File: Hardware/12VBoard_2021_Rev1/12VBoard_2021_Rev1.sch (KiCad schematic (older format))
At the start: 0 parts

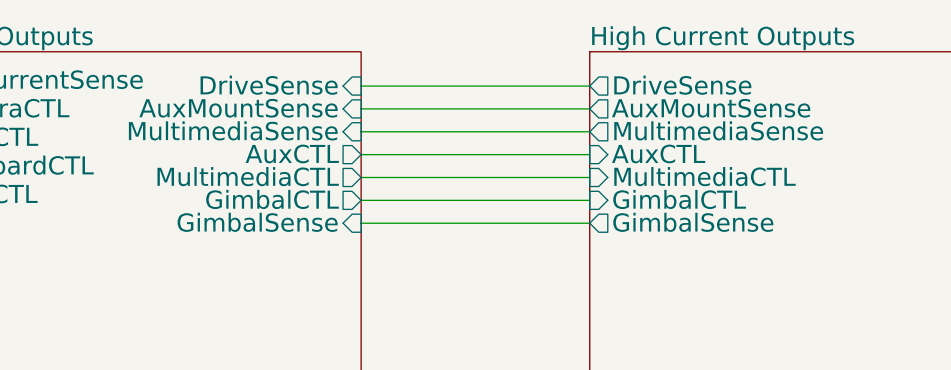
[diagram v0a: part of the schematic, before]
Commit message: Checked H pins
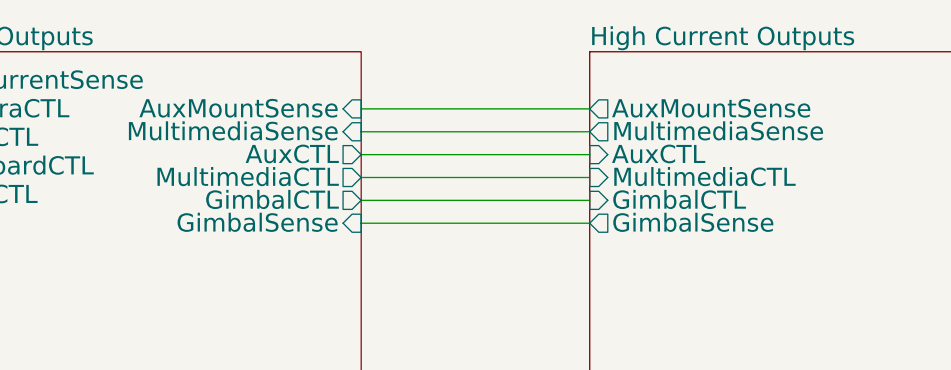
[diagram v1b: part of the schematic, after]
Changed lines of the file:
@@
 EESchema Schematic File Version 4
-LIBS:12VBoard_2021_Rev1-cache
 EELAYER 30 0
 EELAYER END
@@
 F2 "PackVoltage" I L 8000 3900 79
 F3 "5V" I L 8000 3625 79
-F4 "DriveSense" O L 8000 2150 79
-F5 "AuxMountSense" O L 8000 2250 79
-F6 "MultimediaSense" O L 8000 2350 79
-F7 "AuxCTL" I L 8000 2450 79
-F8 "MultimediaCTL" I L 8000 2550 79
-F9 "GimbalCTL" I L 8000 2650 79
-F10 "GimbalSense" O L 8000 2750 79
+F4 "AuxMountSense" O L 8000 2250 79
+F5 "MultimediaSense" O L 8000 2350 79
+F6 "AuxCTL" I L 8000 2450 79
+F7 "MultimediaCTL" I L 8000 2550 79
+F8 "GimbalCTL" I L 8000 2650 79
+F9 "GimbalSense" O L 8000 2750 79
 $EndSheet
 Wire Wire Line
@@
 	4000 2500 5000 2500
 Wire Wire Line
-	7000 2150 8000 2150
-Wire Wire Line
 	7000 2250 8000 2250
-Wire Wire Line
-	7000 2350 8000 2350
 Wire Wire Line
 	7000 2450 8000 2450
@@
 F0 "Tiva In/Outputs" 79
 F1 "Tiva.sch" 79
-F2 "DriveSense" I R 7000 2150 79
-F3 "LowCurrentSense" I L 5000 2125 79
-F4 "AuxMountSense" I R 7000 2250 79
-F5 "CameraCTL" O L 5000 2250 79
-F6 "MultimediaSense" I R 7000 2350 79
-F7 "NavBoardCTL" O L 5000 2500 79
-F8 "AuxCTL" O R 7000 2450 79
-F9 "MultimediaCTL" O R 7000 2550 79
-F10 "ExtraCTL" O L 5000 2625 79
-F11 "GimbalCTL" O R 7000 2650 79
-F12 "GimbalSense" I R 7000 2750 79
-F13 "DriveCTL" O L 5000 2375 79
+F2 "LowCurrentSense" I L 5000 2125 79
+F3 "AuxMountSense" I R 7000 2250 79
+F4 "CameraCTL" O L 5000 2250 79
+F5 "MultimediaSense" I R 7000 2350 79
+F6 "NavBoardCTL" O L 5000 2500 79
+F7 "AuxCTL" O R 7000 2450 79
+F8 "MultimediaCTL" O R 7000 2550 79
+F9 "ExtraCTL" O L 5000 2625 79
+F10 "GimbalCTL" O R 7000 2650 79
+F11 "GimbalSense" I R 7000 2750 79
+F12 "DriveCTL" O L 5000 2375 79
 $EndSheet
+Wire Wire Line
+	7000 2350 8000 2350
 $EndSCHEMATC

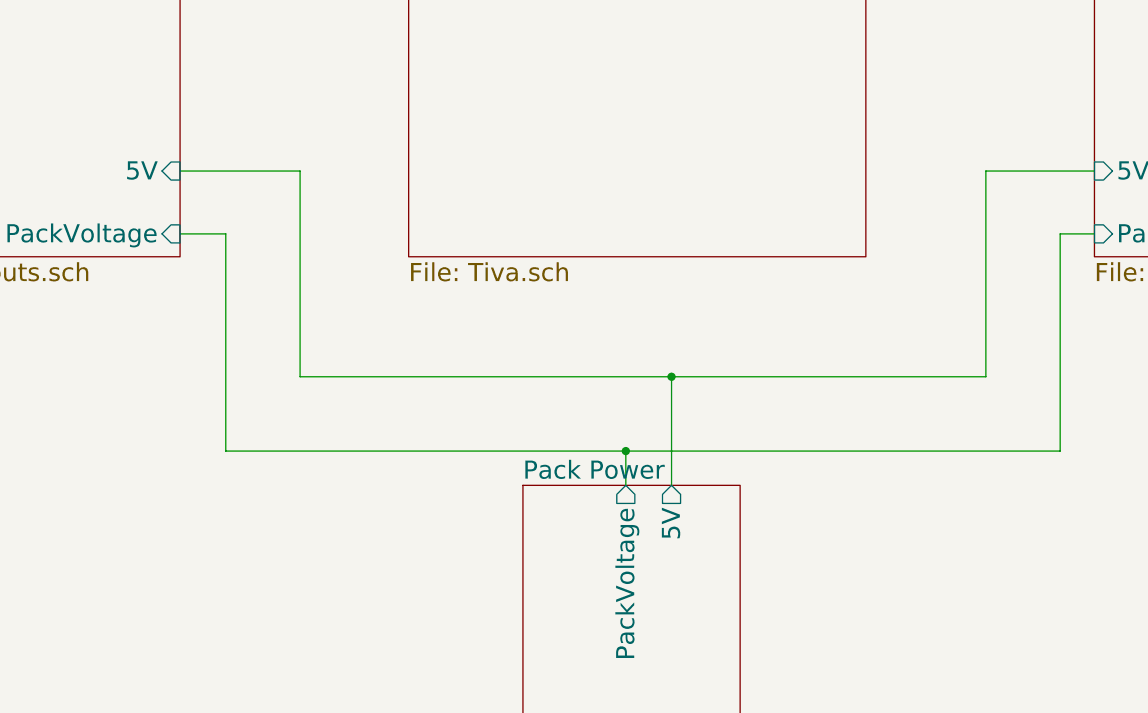
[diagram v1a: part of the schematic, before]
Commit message: Aded oki and started change of high side logic setup
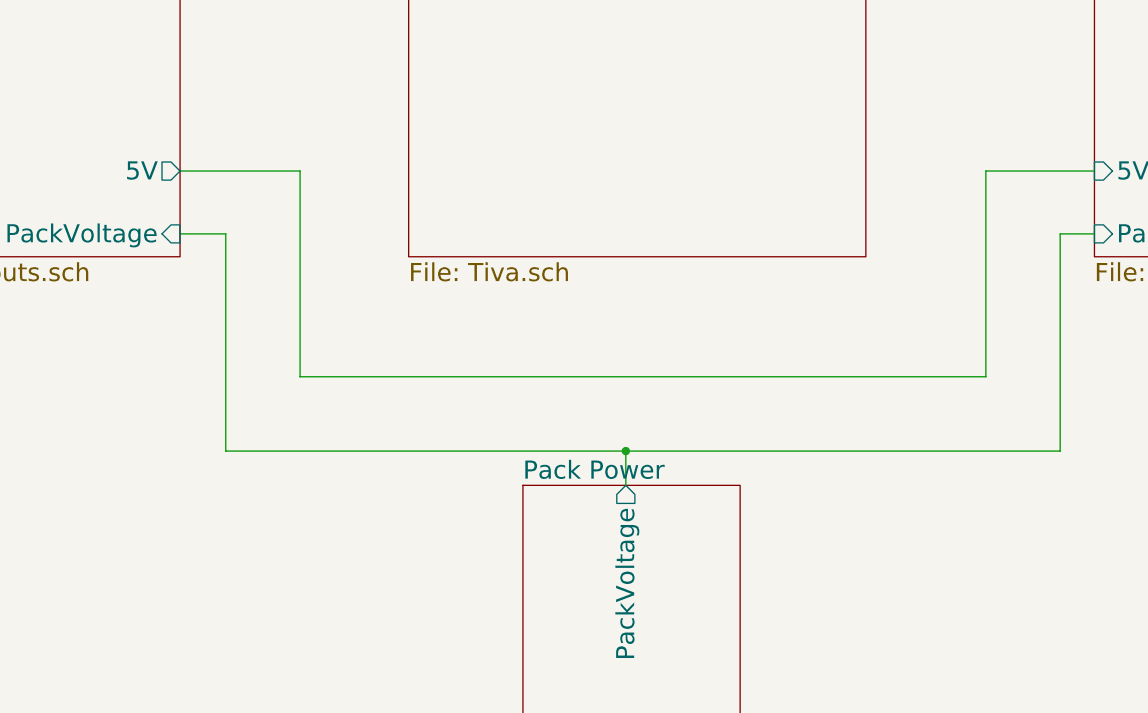
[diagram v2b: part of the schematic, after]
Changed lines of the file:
@@
 F1 "Pack Power.sch" 79
 F2 "PackVoltage" O T 5950 5000 79
-F3 "5V" O T 6150 5000 79
 $EndSheet
 Wire Wire Line
@@
 	7850 3900 8000 3900
 Wire Wire Line
-	6150 5000 6150 4525
-Wire Wire Line
-	6150 4525 4525 4525
-Wire Wire Line
 	4525 4525 4525 3625
 Wire Wire Line
 	4525 3625 4000 3625
-Wire Wire Line
-	6150 4525 7525 4525
-Connection ~ 6150 4525
 Wire Wire Line
 	7525 3625 8000 3625
@@
 F1 "Low Current Outputs.sch" 79
 F2 "PackVoltage" I R 4000 3900 79
-F3 "5V" I R 4000 3625 79
+F3 "5V" O R 4000 3625 79
 F4 "CameraToggle" I R 4000 2250 79
 F5 "NavToggle" I R 4000 2500 79
@@
 Wire Wire Line
 	7000 2350 8000 2350
+Wire Wire Line
+	4525 4525 7525 4525
 $EndSCHEMATC

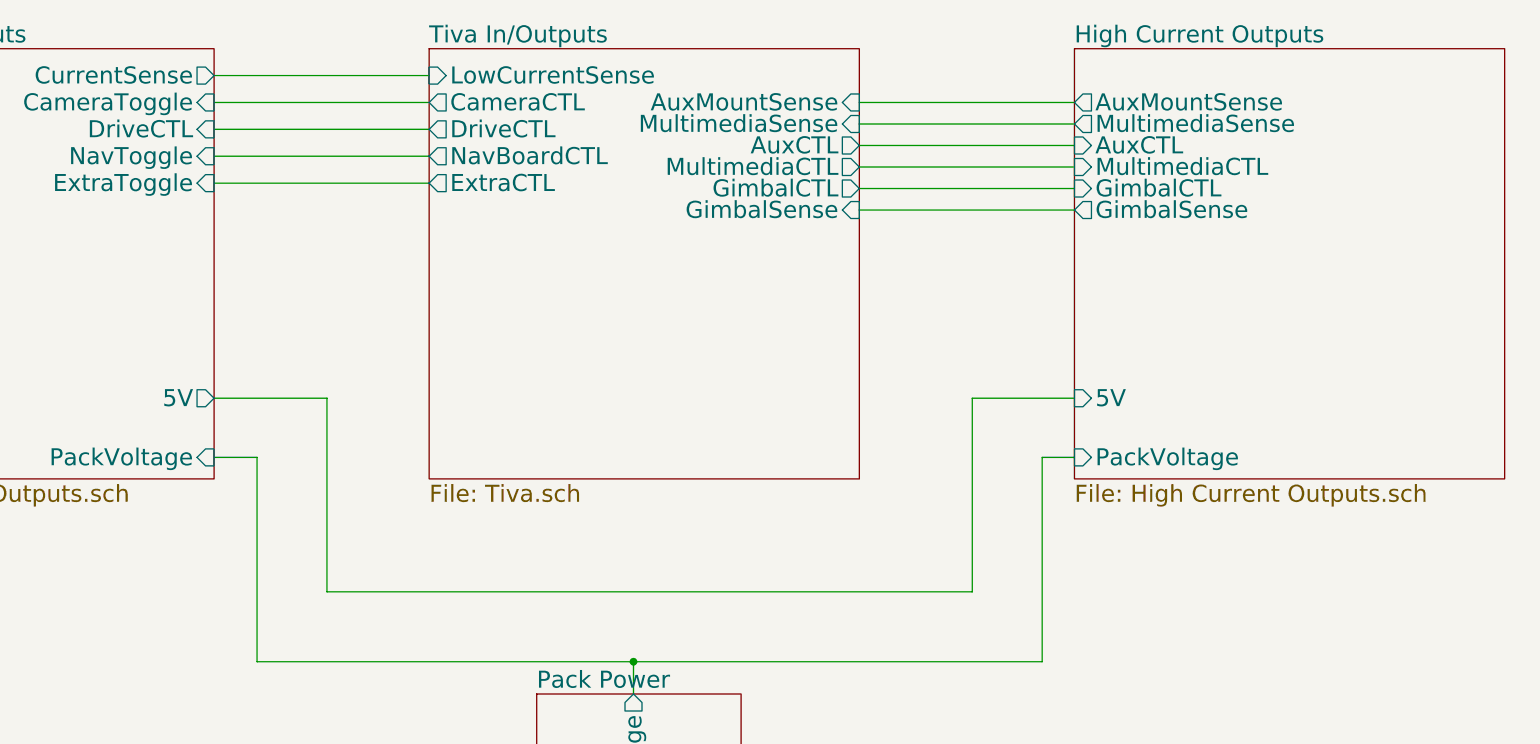
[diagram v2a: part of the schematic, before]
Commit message: Changes!
Added the new correct connectors and redid all signal lines to the High Current side of the board. Also deleted all uncessacary components on the High current side that are no longer used.
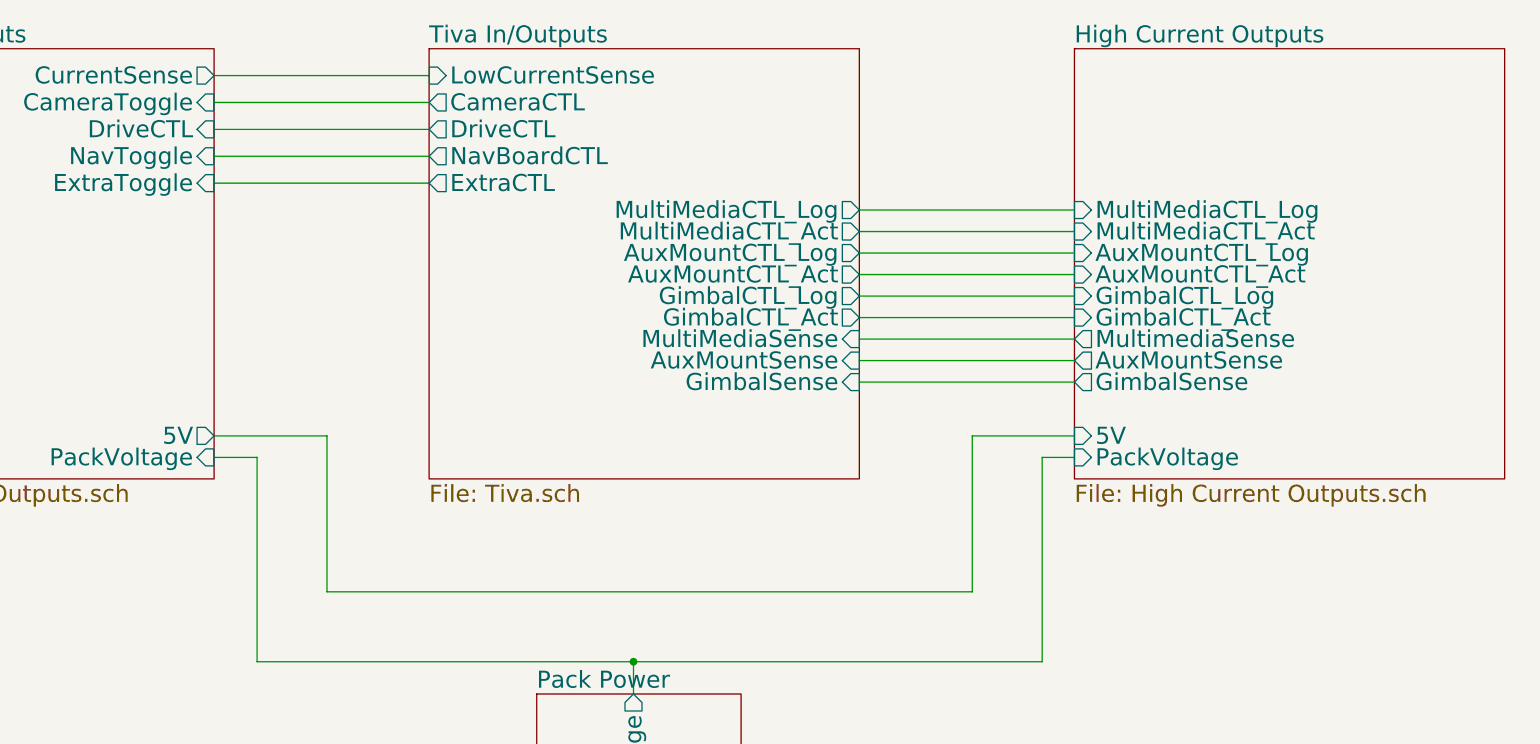
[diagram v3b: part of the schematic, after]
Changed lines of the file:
@@
 $Descr A4 11693 8268
 encoding utf-8
-Sheet 1 8
+Sheet 1 9
 Title ""
 Date ""
@@
 	7850 3900 8000 3900
 Wire Wire Line
-	4525 4525 4525 3625
-Wire Wire Line
-	4525 3625 4000 3625
-Wire Wire Line
-	7525 3625 8000 3625
-Wire Wire Line
-	7525 3625 7525 4525
+	4525 4525 4525 3800
 $Sheet
 S 8000 2000 2000 2000
@@
 F1 "High Current Outputs.sch" 79
 F2 "PackVoltage" I L 8000 3900 79
-F3 "5V" I L 8000 3625 79
-F4 "AuxMountSense" O L 8000 2250 79
-F5 "MultimediaSense" O L 8000 2350 79
-F6 "AuxCTL" I L 8000 2450 79
-F7 "MultimediaCTL" I L 8000 2550 79
-F8 "GimbalCTL" I L 8000 2650 79
-F9 "GimbalSense" O L 8000 2750 79
+F3 "5V" I L 8000 3800 79
+F4 "MultiMediaCTL_Log" I L 8000 2750 79
+F5 "MultiMediaCTL_Act" I L 8000 2850 79
+F6 "AuxMountCTL_Log" I L 8000 2950 79
+F7 "AuxMountCTL_Act" I L 8000 3050 79
+F8 "GimbalCTL_Log" I L 8000 3150 79
+F9 "GimbalCTL_Act" I L 8000 3250 79
+F10 "MultimediaSense" O L 8000 3350 79
+F11 "AuxMountSense" O L 8000 3450 79
+F12 "GimbalSense" O L 8000 3550 79
 $EndSheet
 Wire Wire Line
@@
 	4000 2500 5000 2500
 Wire Wire Line
-	7000 2250 8000 2250
-Wire Wire Line
-	7000 2450 8000 2450
-Wire Wire Line
-	7000 2550 8000 2550
-Wire Wire Line
 	5000 2625 4000 2625
-Wire Wire Line
-	7000 2650 8000 2650
-Wire Wire Line
-	8000 2750 7000 2750
 Wire Wire Line
 	5000 2375 4000 2375
@@
 F1 "Low Current Outputs.sch" 79
 F2 "PackVoltage" I R 4000 3900 79
-F3 "5V" O R 4000 3625 79
+F3 "5V" O R 4000 3800 79
 F4 "CameraToggle" I R 4000 2250 79
 F5 "NavToggle" I R 4000 2500 79
@@
 F1 "Tiva.sch" 79
 F2 "LowCurrentSense" I L 5000 2125 79
-F3 "AuxMountSense" I R 7000 2250 79
-F4 "CameraCTL" O L 5000 2250 79
-F5 "MultimediaSense" I R 7000 2350 79
-F6 "NavBoardCTL" O L 5000 2500 79
-F7 "AuxCTL" O R 7000 2450 79
-F8 "MultimediaCTL" O R 7000 2550 79
-F9 "ExtraCTL" O L 5000 2625 79
-F10 "GimbalCTL" O R 7000 2650 79
-F11 "GimbalSense" I R 7000 2750 79
-F12 "DriveCTL" O L 5000 2375 79
+F3 "CameraCTL" O L 5000 2250 79
+F4 "NavBoardCTL" O L 5000 2500 79
+F5 "ExtraCTL" O L 5000 2625 79
+F6 "DriveCTL" O L 5000 2375 79
+F7 "MultiMediaCTL_Log" O R 7000 2750 79
+F8 "MultiMediaCTL_Act" O R 7000 2850 79
+F9 "AuxMountCTL_Log" O R 7000 2950 79
+F10 "AuxMountCTL_Act" O R 7000 3050 79
+F11 "GimbalCTL_Log" O R 7000 3150 79
+F12 "GimbalCTL_Act" O R 7000 3250 79
+F13 "MultiMediaSense" I R 7000 3350 79
+F14 "AuxMountSense" I R 7000 3450 79
+F15 "GimbalSense" I R 7000 3550 79
 $EndSheet
 Wire Wire Line
-	7000 2350 8000 2350
+	4525 4525 7525 4525
 Wire Wire Line
-	4525 4525 7525 4525
+	8000 3800 7525 3800
+Wire Wire Line
+	7525 3800 7525 4525
+Wire Wire Line
+	4000 3800 4525 3800
+Wire Wire Line
+	7000 2850 8000 2850
+Wire Wire Line
+	7000 2750 8000 2750
+Wire Wire Line
+	7000 2950 8000 2950
+Wire Wire Line
+	7000 3050 8000 3050
+Wire Wire Line
+	7000 3150 8000 3150
+Wire Wire Line
+	7000 3250 8000 3250
+Wire Wire Line
+	7000 3350 8000 3350
+Wire Wire Line
+	7000 3450 8000 3450
+Wire Wire Line
+	7000 3550 8000 3550
 $EndSCHEMATC

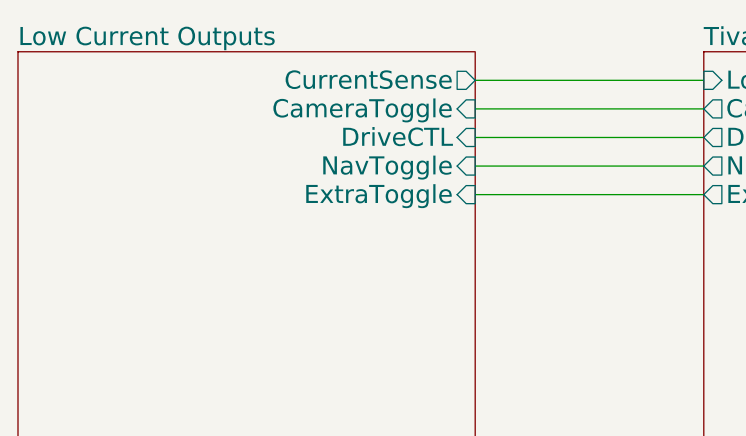
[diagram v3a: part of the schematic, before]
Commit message: Redesigned low current ports schematic
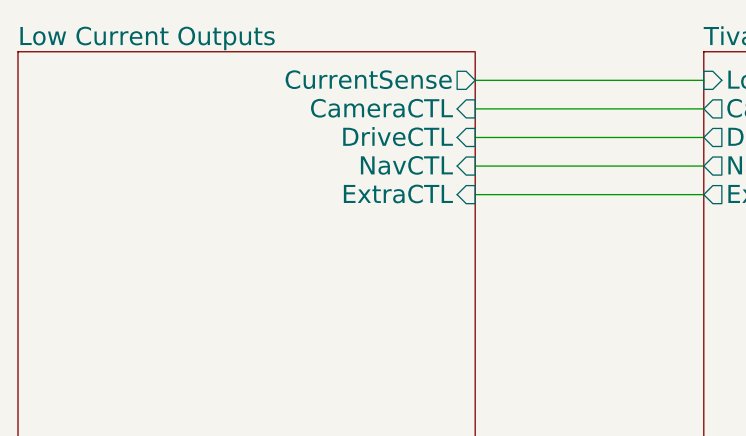
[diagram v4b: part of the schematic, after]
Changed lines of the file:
@@
 F2 "PackVoltage" I R 4000 3900 79
 F3 "5V" O R 4000 3800 79
-F4 "CameraToggle" I R 4000 2250 79
-F5 "NavToggle" I R 4000 2500 79
+F4 "CameraCTL" I R 4000 2250 79
+F5 "NavCTL" I R 4000 2500 79
 F6 "CurrentSense" O R 4000 2125 79
-F7 "ExtraToggle" I R 4000 2625 79
+F7 "ExtraCTL" I R 4000 2625 79
 F8 "DriveCTL" I R 4000 2375 79
 $EndSheet

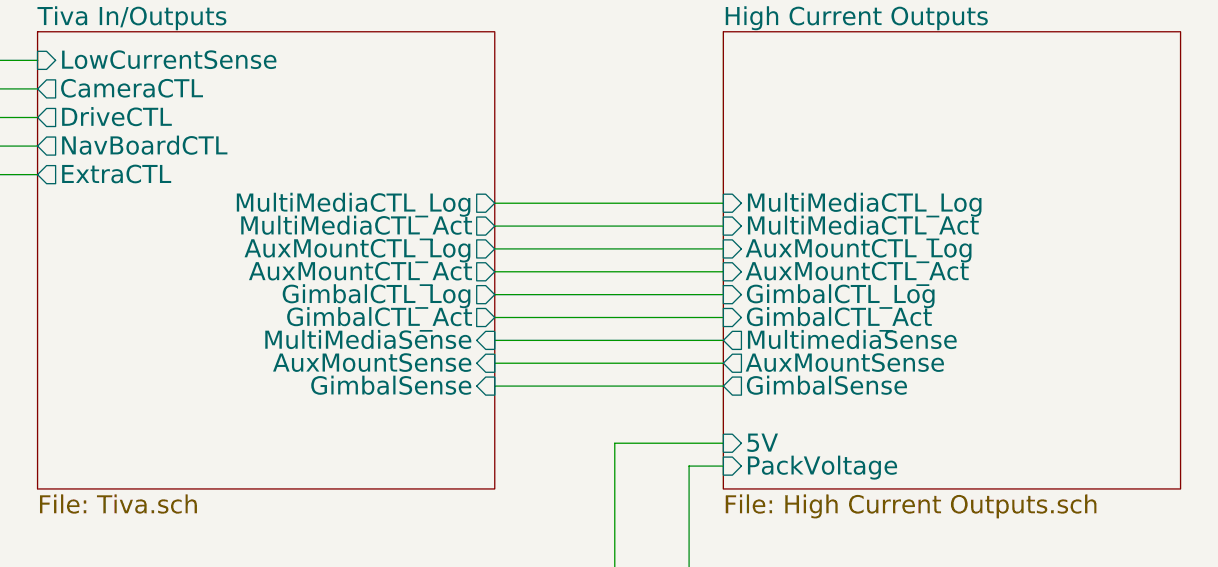
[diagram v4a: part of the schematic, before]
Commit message: changed to big bucks
changed to the bucks used in Master due to a realization in the inductor sizing for the LM5116. It would be much bigger than previous years.
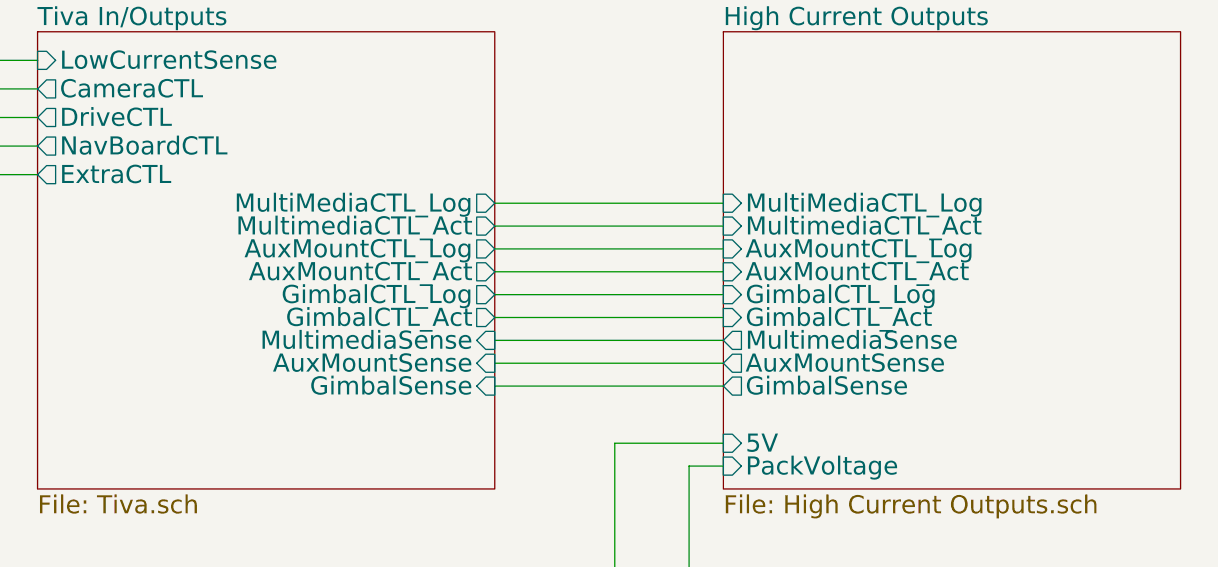
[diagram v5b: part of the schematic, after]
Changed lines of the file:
@@
 $Descr A4 11693 8268
 encoding utf-8
-Sheet 1 9
+Sheet 1 8
 Title ""
 Date ""
@@
 F3 "5V" I L 8000 3800 79
 F4 "MultiMediaCTL_Log" I L 8000 2750 79
-F5 "MultiMediaCTL_Act" I L 8000 2850 79
+F5 "MultimediaCTL_Act" I L 8000 2850 79
 F6 "AuxMountCTL_Log" I L 8000 2950 79
 F7 "AuxMountCTL_Act" I L 8000 3050 79
@@
 F6 "DriveCTL" O L 5000 2375 79
 F7 "MultiMediaCTL_Log" O R 7000 2750 79
-F8 "MultiMediaCTL_Act" O R 7000 2850 79
+F8 "MultimediaCTL_Act" O R 7000 2850 79
 F9 "AuxMountCTL_Log" O R 7000 2950 79
 F10 "AuxMountCTL_Act" O R 7000 3050 79
 F11 "GimbalCTL_Log" O R 7000 3150 79
 F12 "GimbalCTL_Act" O R 7000 3250 79
-F13 "MultiMediaSense" I R 7000 3350 79
+F13 "MultimediaSense" I R 7000 3350 79
 F14 "AuxMountSense" I R 7000 3450 79
 F15 "GimbalSense" I R 7000 3550 79
